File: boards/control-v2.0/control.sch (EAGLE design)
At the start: 107 parts, among them IC1 MCP23017-E/SS, J1 HFW8R-1ST, J2 B2PS-CENTERED-VH(LF)(SN), J3 SBH11-PBPC-D05-RA, J9 DF22-2, U1 TLV70233DBVR, U3 VND5E006ASPTR-E, U4 LMZ14201, U5 MCP1824T-1202E/OT, U6 MCP1824T-2502E/OT, X1 ASV-18.432MHZ-EJ-T

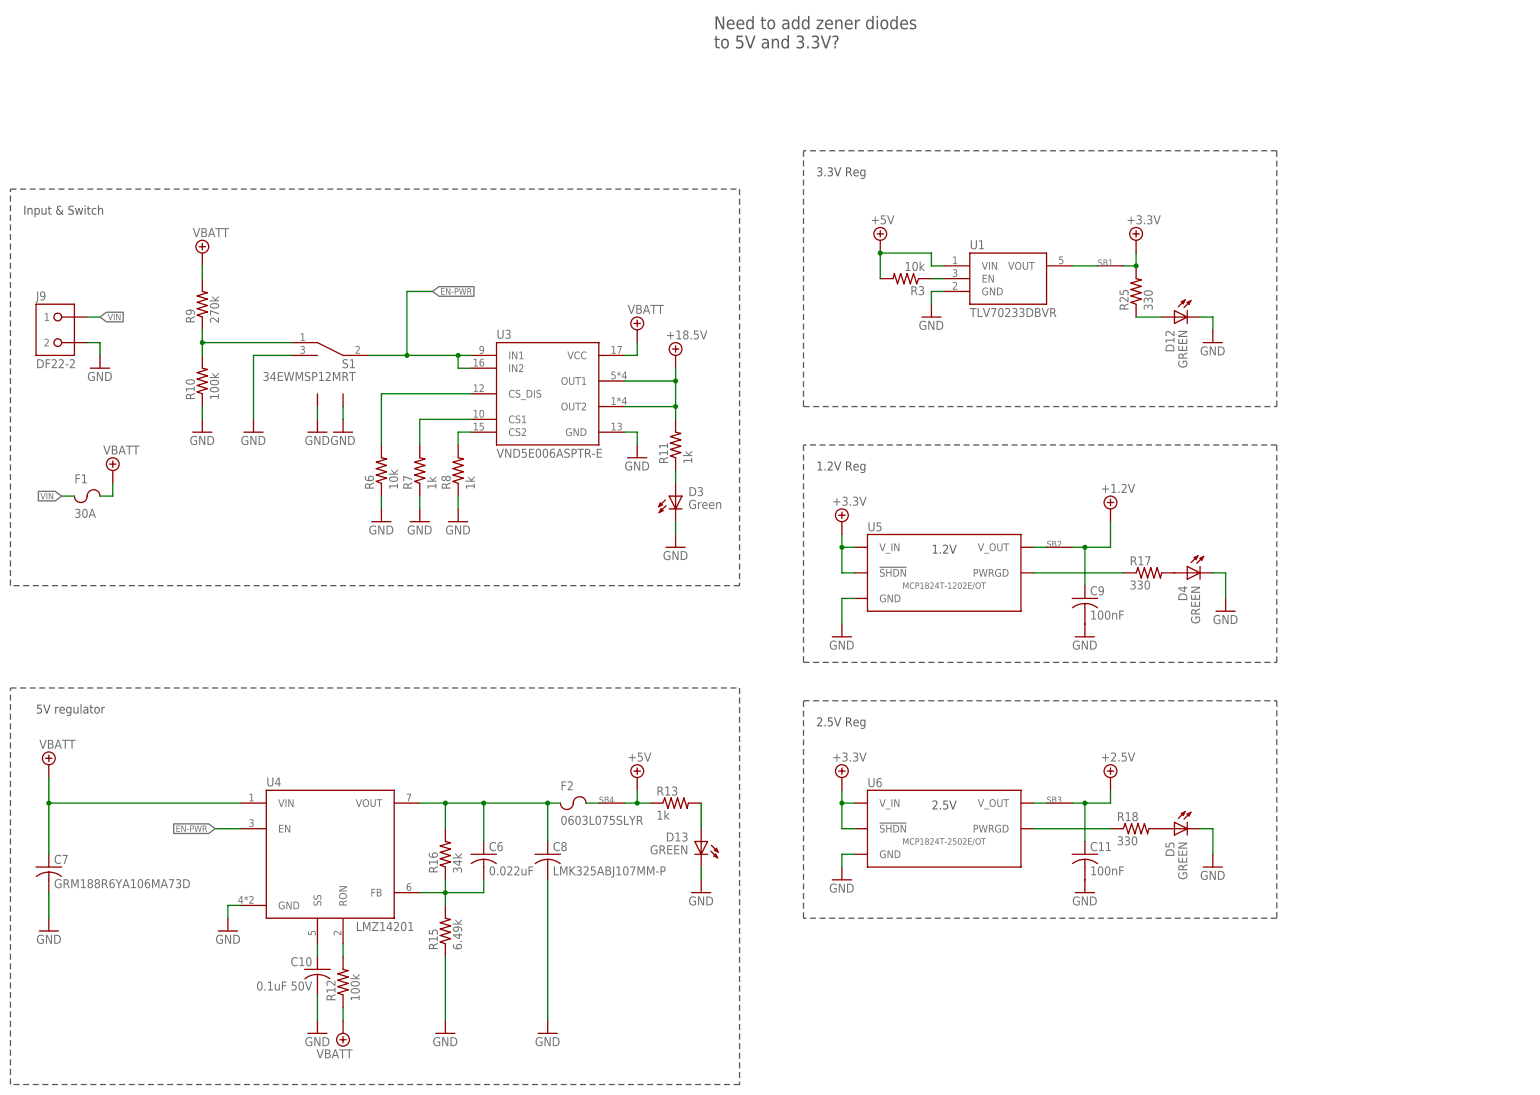
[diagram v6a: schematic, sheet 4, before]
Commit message: Adding MPN for control board parts
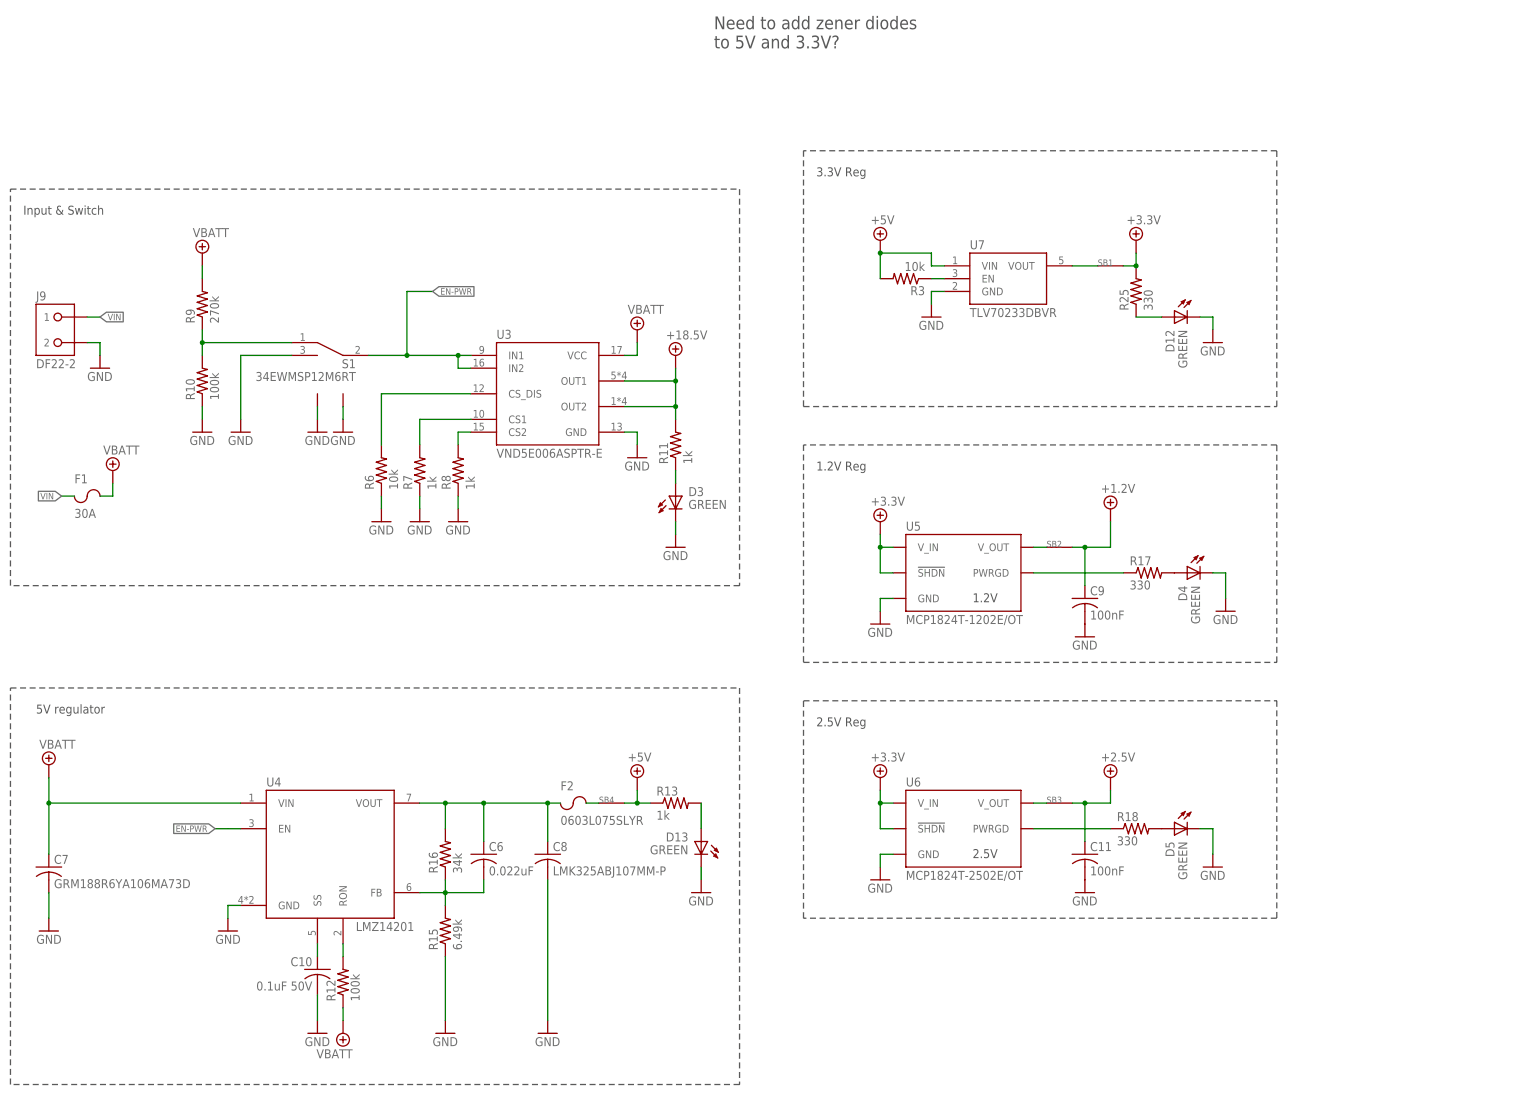
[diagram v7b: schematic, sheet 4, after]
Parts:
- removed U$1: XC3S250E-4TQG144C, RoboJackets-ICs:XC3S250E-4TQG144C
- removed U$2: MPU-6050-1, RoboJackets-Sensors:MPU-6050-1
- added U2: MPU-6050, RoboJackets-Sensors:MPU-6050
- added U7: TLV70233DBVR, RoboJackets-PowerICs:TLV70233DBVR
- D1, D10, D2, D6, D7, D8, D9: device RoboJackets-LEDs:LED_SMD -> RoboJackets-LEDs:LED-SMD-RED
- D11: device RoboJackets-LEDs:LED_SMD -> RoboJackets-LEDs:LED-SMD-BLUE
- D12, D13, D4, D5: device RoboJackets-LEDs:LED_SMD -> RoboJackets-LEDs:LED-SMD-GREEN
- D3: value Green -> GREEN; device RoboJackets-LEDs:LED_SMD -> RoboJackets-LEDs:LED-SMD-GREEN
- J2: value B2PS-CENTERED-VH(LF)(SN) -> B2PS-VH(LF)(SN); device RoboJackets-Connectors:B2PS-CENTERED-VH(LF)(SN) -> RoboJackets-Connectors:B2PS-VH(LF)(SN)
- RN1, RN11, RN14, RN17, RN2, RN3, RN4, RN5, RN6, RN7, RN8, RN9: value 742C163331JP -> (none); device RoboJackets-Resistors:742C163331JP -> RoboJackets-Resistors:RA-8
- S1: value 34EWMSP12MRT -> 34EWMSP12M6RT; device RoboJackets-Switches:34EWMSP12MRT -> RoboJackets-Switches:34EWMSP12M6RT
- S3: DIGIKEY (none) -> CT2193MST-ND; MPN (none) -> 219-3MST
- U1: value TLV70233DBVR -> XC3S250E-4TQG144C; device RoboJackets-PowerICs:TLV70233DBVR -> RoboJackets-ICs:XC3S250E-4TQG144C
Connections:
- net !CS!-FPGA: now also U1.69_IP; no longer U$1.69_IP
- net +1.2V: now also U1.115_VCCINT, U1.45_VCCINT, U1.80_VCCINT, U1.9_VCCINT; no longer U$1.115_VCCINT, U$1.45_VCCINT, U$1.80_VCCINT, U$1.9_VCCINT
- net +2.5V: now also U1.102_VCCAUX, U1.137_VCCAUX, U1.30_VCCAUX, U1.65_VCCAUX; no longer U$1.102_VCCAUX, U$1.137_VCCAUX, U$1.30_VCCAUX, U$1.65_VCCAUX
- net +3.3V: now also U1.100_VCCO_1, U1.121_VCCO_0, U1.138_VCCO_0, U1.13_VCCO_3, U1.143_IO_L10N_0/HSWAP, U1.28_VCCO_3, U1.42_VCCO_2, U1.49_VCCO_2, U1.60_IO/M1, U1.62_IO_L08P_2/M0, U1.64_VCCO_2, U1.79_VCCO_1, U2.VDD, U2.VLOGIC; no longer U$1.100_VCCO_1, U$1.121_VCCO_0, U$1.138_VCCO_0, U$1.13_VCCO_3, U$1.143_IO_L10N_0/HSWAP, U$1.28_VCCO_3, U$1.42_VCCO_2, U$1.49_VCCO_2, U$1.60_IO/M1, U$1.62_IO_L08P_2/M0, U$1.64_VCCO_2, U$1.79_VCCO_1, U$2.VDD, U$2.VLOGIC
- net +3.3V-PRE: now also U7.VOUT; no longer U1.VOUT
- net +5V: now also U7.VIN; no longer U1.VIN
- net FPGA-CLK: now also U1.50_IO_L04P_2/D7/GCLK12; no longer U$1.50_IO_L04P_2/D7/GCLK12
- net FPGA-DONE: now also U1.72_DONE; no longer U$1.72_DONE
- net FPGA-INIT: now also U1.40_IO_L01N_2/INIT_B; no longer U$1.40_IO_L01N_2/INIT_B
- net FPGA-PROG: now also U1.1_PROGB; no longer U$1.1_PROGB
- net GND: now also U1.118_GND, U1.11_GND, U1.127_GND, U1.133_GND, U1.19_GND, U1.27_GND, U1.37_GND, U1.46_GND, U1.55_GND, U1.61_GND, U1.73_GND, U1.90_GND, U1.99_GND, U2.AD0, U2.CLKIN, U2.FSYNC, U2.GND, U7.GND; no longer U$1.118_GND, U$1.11_GND, U$1.127_GND, U$1.133_GND, U$1.19_GND, U$1.27_GND, U$1.37_GND, U$1.46_GND, U$1.55_GND, U$1.61_GND, U$1.73_GND, U$1.90_GND, U$1.99_GND, U$2.AD0, U$2.CLKIN, U$2.FSYNC, U$2.GND
- net INT-MPU: now also U2.INT; no longer U$2.INT
- net MISO: now also U1.63_IO_L08N_2/DIN/D0; no longer U$1.63_IO_L08N_2/DIN/D0
- net MOSI: now also U1.44_IO_L02N_2/MOSI/CSI_B; no longer U$1.44_IO_L02N_2/MOSI/CSI_B
- net N$91: now also U2.REGOUT; no longer U$2.REGOUT
- net N$92: now also U2.CPOUT; no longer U$2.CPOUT
- net N$93: now also U7.EN; no longer U1.EN
- net R-P1: now also U1.82_IO_L03N_1/A11; no longer U$1.82_IO_L03N_1/A11
- net R-P10: now also U1.89_IP; no longer U$1.89_IP
- net R-P11: now also U1.88_IO_L05N_1/A7/RHCLK3; no longer U$1.88_IO_L05N_1/A7/RHCLK3
- net R-P12: now also U1.87_IO_L05P_1/A8/RHCLK2; no longer U$1.87_IO_L05P_1/A8/RHCLK2
- net R-P13: now also U1.86_IO_L04N_1/A9/RHCLK1; no longer U$1.86_IO_L04N_1/A9/RHCLK1
- net R-P14: now also U1.85_IO_L04P_1/A10/RHCLK0; no longer U$1.85_IO_L04P_1/A10/RHCLK0
- net R-P15: now also U1.84_IP; no longer U$1.84_IP
- net R-P16: now also U1.83_IO/VREF_1; no longer U$1.83_IO/VREF_1
- net R-P17: now also U1.101_IP; no longer U$1.101_IP
- net R-P18: now also U1.98_IO/A0; no longer U$1.98_IO/A0
- net R-P19: now also U1.97_IO_L08N_1/A1; no longer U$1.97_IO_L08N_1/A1
- net R-P2: now also U1.81_IO_L03P_1/A12; no longer U$1.81_IO_L03P_1/A12
- net R-P20: now also U1.96_IO_L08P_1/A2; no longer U$1.96_IO_L08P_1/A2
- net R-P21: now also U1.95_IP/VREF_1; no longer U$1.95_IP/VREF_1
- net R-P22: now also U1.94_IO_L07N_1/A3/RHCLK7; no longer U$1.94_IO_L07N_1/A3/RHCLK7
- net R-P23: now also U1.93_IO_L07P_1/A4/RHCLK6; no longer U$1.93_IO_L07P_1/A4/RHCLK6
- net R-P24: now also U1.92_IO_L06N_1/A5/RHCLK5; no longer U$1.92_IO_L06N_1/A5/RHCLK5
- net R-P25: now also U1.117_IO_L02N_0; no longer U$1.117_IO_L02N_0
- net R-P26: now also U1.116_IO_L02P_0; no longer U$1.116_IO_L02P_0
- net R-P27: now also U1.113_IO_L01N_0; no longer U$1.113_IO_L01N_0
- net R-P28: now also U1.112_IO_L01P_0; no longer U$1.112_IO_L01P_0
- net R-P29: now also U1.106_IO_L10N_1/LDC2; no longer U$1.106_IO_L10N_1/LDC2
- net R-P3: now also U1.77_IO_L02N_1/A13; no longer U$1.77_IO_L02N_1/A13
- net R-P30: now also U1.105_IO_L10P_1/LDC1; no longer U$1.105_IO_L10P_1/LDC1
- net R-P31: now also U1.104_IO_L09N_1/LDC0; no longer U$1.104_IO_L09N_1/LDC0
- net R-P32: now also U1.103_IO_L09P_1/HDC; no longer U$1.103_IO_L09P_1/HDC
- net R-P36: now also U1.125_IO_L05P_0/GCLK6; no longer U$1.125_IO_L05P_0/GCLK6
- net R-P37: now also U1.124_IO/VREF_0; no longer U$1.124_IO/VREF_0
- net R-P38: now also U1.123_IO_L04N_0/GCLK5; no longer U$1.123_IO_L04N_0/GCLK5
- net R-P39: now also U1.122_IO_L04P_0/GCLK4; no longer U$1.122_IO_L04P_0/GCLK4
- net R-P4: now also U1.76_IO_L02P_1/A14; no longer U$1.76_IO_L02P_1/A14
- net R-P40: now also U1.119_IP_L03P_0; no longer U$1.119_IP_L03P_0
- net R-P41: now also U1.5_IOL02N_3/VREF_3; no longer U$1.5_IOL02N_3/VREF_3
- net R-P42: now also U1.4_IOL02P_3; no longer U$1.4_IOL02P_3
- net R-P43: now also U1.3_IOL01N_3; no longer U$1.3_IOL01N_3
- net R-P44: now also U1.2_IOL01P_3; no longer U$1.2_IOL01P_3
- net R-P45: now also U1.142_IO_L10P_0; no longer U$1.142_IO_L10P_0
- net R-P46: now also U1.141_IP; no longer U$1.141_IP
- net R-P47: now also U1.140_IO_L09N_0; no longer U$1.140_IO_L09N_0
- net R-P48: now also U1.139_IO_L09P_0; no longer U$1.139_IO_L09P_0
- net R-P49: now also U1.21_IO_L06N_3/LHCLK5; no longer U$1.21_IO_L06N_3/LHCLK5
- net R-P5: now also U1.75_IO_L01N_1/A15; no longer U$1.75_IO_L01N_1/A15
- net R-P50: now also U1.20_IO_L06P_3/LHCLK4; no longer U$1.20_IO_L06P_3/LHCLK4
- net R-P51: now also U1.17_IO_L05N_3/LHCLK3; no longer U$1.17_IO_L05N_3/LHCLK3
- net R-P52: now also U1.16_IO_L05P_3/LHCLK2; no longer U$1.16_IO_L05P_3/LHCLK2
- net R-P53: now also U1.15_IO_L04N_3/LHCLK1; no longer U$1.15_IO_L04N_3/LHCLK1
- net R-P54: now also U1.14_IO_L04P_3/LHCLK0; no longer U$1.14_IO_L04P_3/LHCLK0
- net R-P55: now also U1.8_IOL03N_3; no longer U$1.8_IOL03N_3
- net R-P56: now also U1.7_IOL03P_3; no longer U$1.7_IOL03P_3
- net R-P57: now also U1.35_IO_L10N_3; no longer U$1.35_IO_L10N_3
- net R-P58: now also U1.34_IO_L10P_3; no longer U$1.34_IO_L10P_3
- net R-P59: now also U1.32_IO_L09P_3; no longer U$1.32_IO_L09P_3
- net R-P6: now also U1.74_IO_L01P_1/A16; no longer U$1.74_IO_L01P_1/A16
- net R-P60: now also U1.31_IO/VREF_3; no longer U$1.31_IO/VREF_3
- net R-P61: now also U1.26_IO_L08N_3; no longer U$1.26_IO_L08N_3
- net R-P62: now also U1.25_IO_L08P_3; no longer U$1.25_IO_L08P_3
- net R-P63: now also U1.24_IP; no longer U$1.24_IP
- net R-P64: now also U1.23_IO_L07N_3/LHCLK7; no longer U$1.23_IO_L07N_3/LHCLK7
- net R-P7: now also U1.70_IO_L10P_2/VS0/A17; no longer U$1.70_IO_L10P_2/VS0/A17
- net R-P8: now also U1.68_IO_L09N_2/VS1/A18; no longer U$1.68_IO_L09N_2/VS1/A18
- net R-P9: now also U1.91_IO_L06P_1/A6/RHCLK4; no longer U$1.91_IO_L06P_1/A6/RHCLK4
- net SCK: now also U1.71_IO_L10N_2/CCLK; no longer U$1.71_IO_L10N_2/CCLK
- net SCL: now also U2.SCL; no longer U$2.SCL
- net SDA: now also U2.SDA; no longer U$2.SDA
- net TCK: now also U1.110_TCK; no longer U$1.110_TCK
- net TDO: now also U1.109_TDO; no longer U$1.109_TDO
- net TMS: now also U1.108_TMS; no longer U$1.108_TMS
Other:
- moved on the sheet: C34, U5, U6

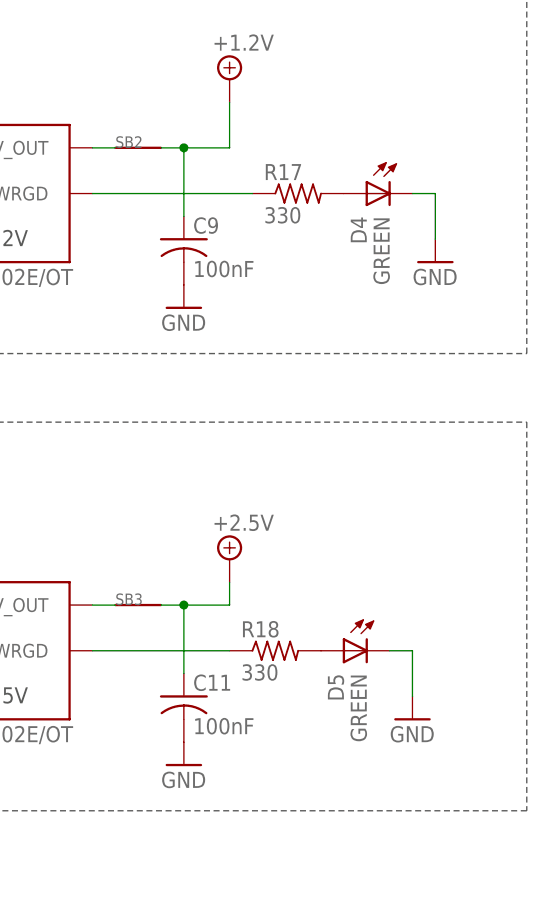
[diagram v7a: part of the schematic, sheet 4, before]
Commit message: Rename nets
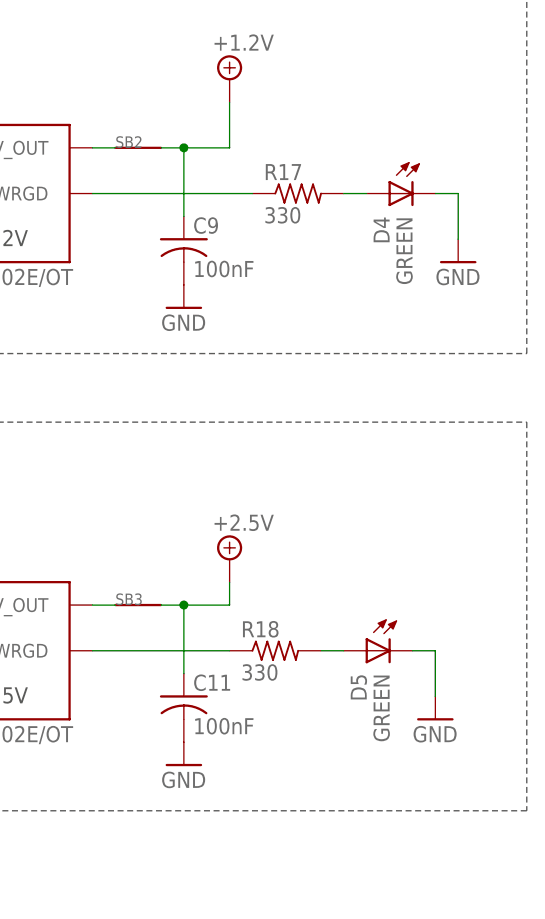
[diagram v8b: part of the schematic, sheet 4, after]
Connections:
- net N$10 renamed GL-B
- net N$12 renamed GH-B
- net N$13 renamed BST-A
- net N$14 renamed BST-B
- net N$16 renamed GL-C
- net N$17 renamed GH-C
- net N$18 renamed BST-C
- net N$19 renamed EN-GATE
- net N$33 renamed LED-BALL-PRE
- net N$34 renamed 1.2V-LED-PRE
- net N$35 renamed 1.2V-LED
- net N$36 renamed 2.5V-LED-PRE
- net N$37 renamed 2.5V-LED
- net N$38 renamed 3.3V-LED-PRE
- net N$39 renamed 5V-LED-PRE
- net N$40 renamed +5V-PRE
- net N$5 renamed GPB4
- net N$68 renamed CS2
- net N$69 renamed CS1
- net N$7 renamed GPB6
- net N$70 renamed CS-DIS
- net N$71 renamed EN-PWR-PRE
- net N$72 renamed 18.5V-LED-PRE
- net N$74 renamed SS
- net N$75 renamed RON
- net N$77 renamed FB
- net N$78 renamed +5V-FUSE
- net N$91 renamed REGOUT
- net N$92 renamed CPOUT
- net N$93 renamed 3.3V-EN
- removed net N$1: C2.1, IC1.GPB0, RN1.8, U1.AVDD
- removed net N$2: C3.1, IC1.GPB1, RN1.7, U1.CP1
- removed net N$3: C3.2, IC1.GPB2, RN1.6, U1.CP2
- removed net N$4: C9.1, IC1.GPB3, RN1.5, U1.GVDD
- removed net N$6: IC1.GPB5, RN1.3, U1.GL_A
- removed net N$8: IC1.GPB7, RN1.1, U1.GH_A
- new net AVDD: C2.1, U1.AVDD
- new net CP1: C3.1, U1.CP1
- new net CP2: C3.2, U1.CP2
- new net GH-A: U1.GH_A
- new net GL-A: U1.GL_A
- new net GPB0: IC1.GPB0, RN1.8
- new net GPB1: IC1.GPB1, RN1.7
- new net GPB2: IC1.GPB2, RN1.6
- new net GPB3: IC1.GPB3, RN1.5
- new net GPB5: IC1.GPB5, RN1.3
- new net GPB7: IC1.GPB7, RN1.1
- new net GVDD: C9.1, U1.GVDD
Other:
- moved on the sheet: D11, D4, D5
